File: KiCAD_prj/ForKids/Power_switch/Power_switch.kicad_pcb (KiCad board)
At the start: 2 copper layers, 61 x 33 mm, 19 parts, among them J1 Screw_Terminal_01x02, J2 Conn_01x04_Female, J3 Conn_01x04_Female, J4 Conn_01x04_Female, J5 Conn_01x04_Female, J6 Conn_01x04_Female, J7 Conn_01x04_Female, SW1 SW_SPST, U1 AMS1117-3.3, U2 AMS1117-5.0

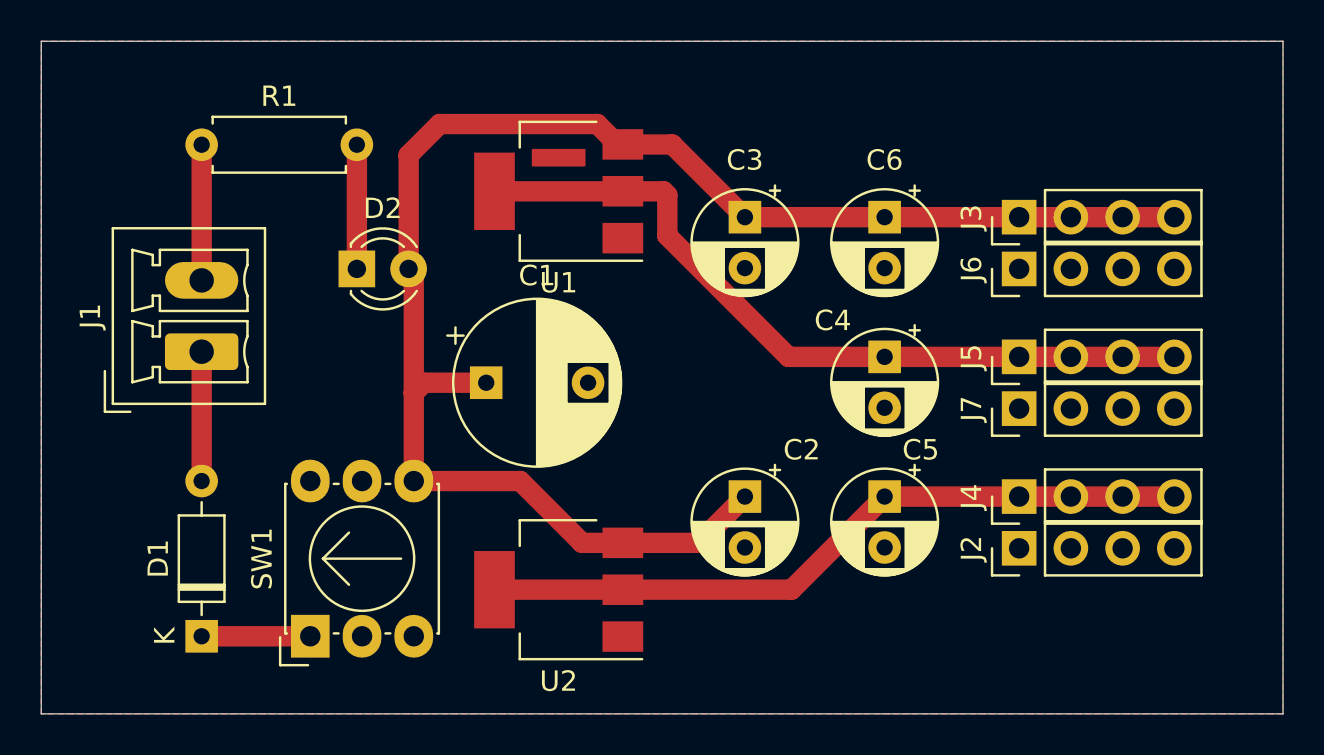
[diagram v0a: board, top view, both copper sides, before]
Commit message: Update Power Switch project KiCAD
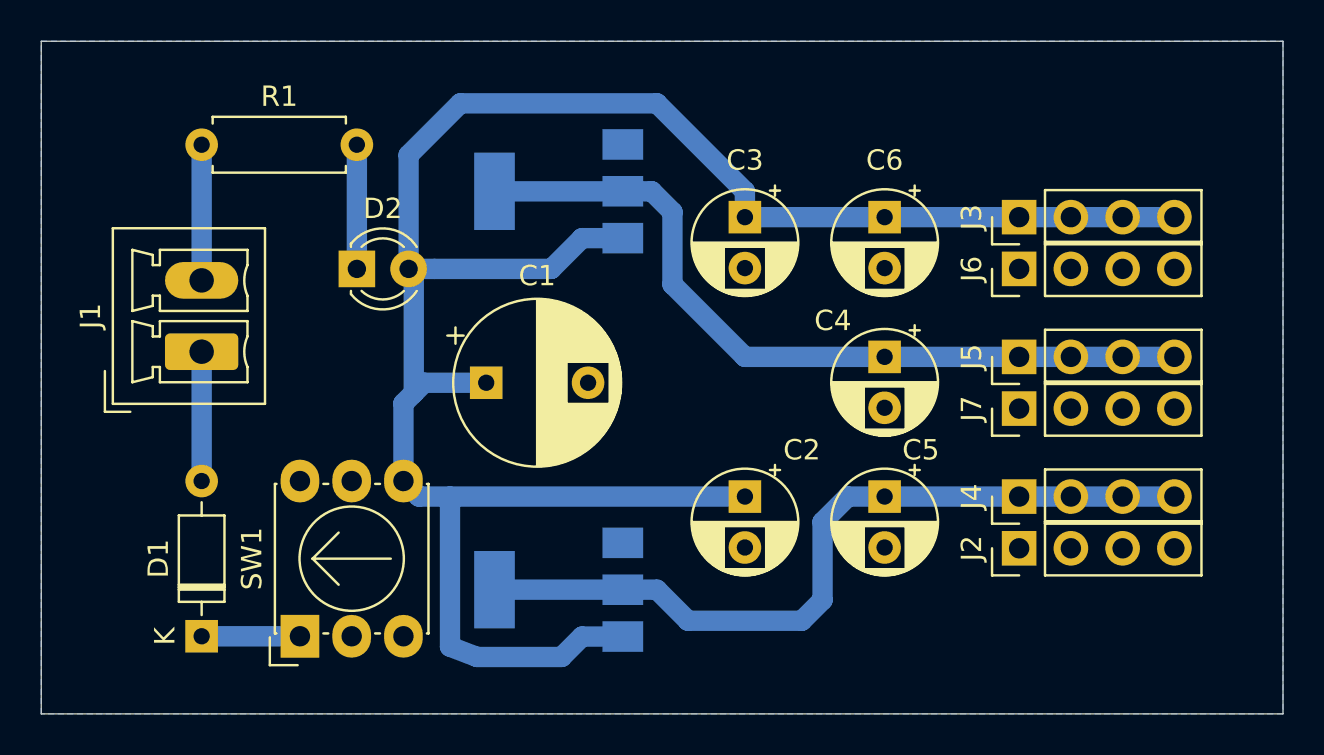
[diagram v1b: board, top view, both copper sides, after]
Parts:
- U1, U2: moved to B.Cu
- moved SW1 0.51 mm to (12.7, -3.81)
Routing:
- net VCC: track 78.4 -> 106.4 mm
- net Net-(C5-Pad1): track 35.3 -> 38.1 mm
- net Net-(C4-Pad1): track 37.9 -> 38.8 mm
- net Net-(D1-Pad1): track 5.33 -> 4.83 mm
- added copper zone on B.Cu, net Earth
- removed copper zone on F.Cu, net Earth

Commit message: Many changes
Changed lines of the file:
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@@
   (layers
     (0 F.Cu signal hide)
-    (31 B.Cu signal)
+    (31 B.Cu signal hide)
     (32 B.Adhes user hide)
     (33 F.Adhes user hide)
@@
       (effects (font (size 1 1) (thickness 0.15)))
     )
-    (fp_text value 10uF (at 1.25 3.75 90) (layer F.Fab)
+    (fp_text value 10uF (at -4.572 0.254 180) (layer F.Fab)
       (effects (font (size 1 1) (thickness 0.15)))
     )
@@
       (effects (font (size 1 1) (thickness 0.15)))
     )
-    (fp_text value 10uF (at 1.25 3.75 90) (layer F.Fab)
+    (fp_text value 10uF (at 5.588 -0.254 180) (layer F.Fab)
       (effects (font (size 1 1) (thickness 0.15)))
     )
@@
     (descr "Through hole straight pin header, 1x04, 2.54mm pitch, single row")
     (tags "Through hole pin header THT 1x04 2.54mm single row")
-    (fp_text reference J7 (at 0 -2.33 90) (layer F.SilkS)
+    (fp_text reference J7 (at 0 -2.794 180) (layer F.SilkS)
       (effects (font (size 1 1) (thickness 0.15)))
     )
@@
       (effects (font (size 1 1) (thickness 0.15)))
     )
-    (fp_text user %R (at 0 3.81) (layer F.Fab)
+    (fp_text user %R (at 0 3.81) (layer F.Fab) hide
       (effects (font (size 1 1) (thickness 0.15)))
     )
@@
     (descr "Through hole straight pin header, 1x04, 2.54mm pitch, single row")
     (tags "Through hole pin header THT 1x04 2.54mm single row")
-    (fp_text reference J6 (at 0 -2.33 90) (layer F.SilkS)
+    (fp_text reference J6 (at 0 -2.794 180) (layer F.SilkS)
       (effects (font (size 1 1) (thickness 0.15)))
     )
@@
       (effects (font (size 1 1) (thickness 0.15)))
     )
-    (fp_text user %R (at 0 3.81) (layer F.Fab)
+    (fp_text user %R (at 0 3.81) (layer F.Fab) hide
       (effects (font (size 1 1) (thickness 0.15)))
     )
@@
     (descr "Through hole straight pin header, 1x04, 2.54mm pitch, single row")
     (tags "Through hole pin header THT 1x04 2.54mm single row")
-    (fp_text reference J5 (at 0 -2.33 90) (layer F.SilkS)
+    (fp_text reference J5 (at 0 -2.794 180) (layer F.SilkS)
       (effects (font (size 1 1) (thickness 0.15)))
     )
@@
       (effects (font (size 1 1) (thickness 0.15)))
     )
-    (fp_text user %R (at 0 3.81) (layer F.Fab)
+    (fp_text user %R (at 0 3.81) (layer F.Fab) hide
       (effects (font (size 1 1) (thickness 0.15)))
     )
@@
     (descr "Through hole straight pin header, 1x04, 2.54mm pitch, single row")
     (tags "Through hole pin header THT 1x04 2.54mm single row")
-    (fp_text reference J4 (at 0 -2.33 90) (layer F.SilkS)
+    (fp_text reference J4 (at 0 -2.794 180) (layer F.SilkS)
       (effects (font (size 1 1) (thickness 0.15)))
     )
@@
       (effects (font (size 1 1) (thickness 0.15)))
     )
-    (fp_text user %R (at 0 3.81) (layer F.Fab)
+    (fp_text user %R (at 0 3.81) (layer F.Fab) hide
       (effects (font (size 1 1) (thickness 0.15)))
     )
@@
     (descr "Through hole straight pin header, 1x04, 2.54mm pitch, single row")
     (tags "Through hole pin header THT 1x04 2.54mm single row")
-    (fp_text reference J3 (at 0 -2.33 90) (layer F.SilkS)
+    (fp_text reference J3 (at 0 -2.794 180) (layer F.SilkS)
       (effects (font (size 1 1) (thickness 0.15)))
     )
@@
       (effects (font (size 1 1) (thickness 0.15)))
     )
-    (fp_text user %R (at 0 3.81) (layer F.Fab)
+    (fp_text user %R (at 0 3.81) (layer F.Fab) hide
       (effects (font (size 1 1) (thickness 0.15)))
     )
@@
     (descr "Through hole straight pin header, 1x04, 2.54mm pitch, single row")
     (tags "Through hole pin header THT 1x04 2.54mm single row")
-    (fp_text reference J2 (at 0 -2.33 90) (layer F.SilkS)
+    (fp_text reference J2 (at 0 -2.794 180) (layer F.SilkS)
       (effects (font (size 1 1) (thickness 0.15)))
     )
@@
       (effects (font (size 1 1) (thickness 0.15)))
     )
-    (fp_text user %R (at 0 3.81) (layer F.Fab)
+    (fp_text user %R (at 0 3.81) (layer F.Fab) hide
       (effects (font (size 1 1) (thickness 0.15)))
     )
@@
       (effects (font (size 1 1) (thickness 0.15)))
     )
-    (fp_text value SW_SPST (at 3.81 7.44 90) (layer F.Fab)
-      (effects (font (size 1 1) (thickness 0.15)))
-    )
-    (fp_text user %R (at 3.81 2.54 90) (layer F.Fab)
+    (fp_text value SW_SPST (at 3.81 7.44 90) (layer F.Fab) hide
+      (effects (font (size 1 1) (thickness 0.15)))
+    )
+    (fp_text user %R (at 3.556 8.382 180) (layer F.Fab)
       (effects (font (size 1 1) (thickness 0.15)))
     )
@@
     (descr "Generic Phoenix Contact connector footprint for: MCV_1,5/2-G-3.5; number of pins: 02; pin pitch: 3.50mm; Vertical || order number: 1843606 8A 160V")
     (tags "phoenix_contact connector MCV_01x02_G_3.5mm")
-    (fp_text reference J1 (at 1.75 -5.45 90) (layer F.SilkS)
+    (fp_text reference J1 (at 1.75 -5.45 180) (layer F.SilkS)
       (effects (font (size 1 1) (thickness 0.15)))
     )
@@
       (effects (font (size 1 1) (thickness 0.15)))
     )
-    (fp_text user %R (at 1.75 -3.55 90) (layer F.Fab)
+    (fp_text user %R (at 1.75 -3.55 90) (layer F.Fab) hide
       (effects (font (size 1 1) (thickness 0.15)))
     )
@@
       (effects (font (size 1 1) (thickness 0.15)))
     )
-    (fp_text value 1N4148 (at 4.318 -3.81 90) (layer F.Fab)
+    (fp_text value 1N4148 (at 9.906 0.254 180) (layer F.Fab)
       (effects (font (size 1 1) (thickness 0.15)))
     )
@@
       (effects (font (size 1 1) (thickness 0.15)))
     )
-    (fp_text value 22uF (at 1.25 3.75 90) (layer F.Fab)
+    (fp_text value 22uF (at -4.572 0 180) (layer F.Fab)
       (effects (font (size 1 1) (thickness 0.15)))
     )
@@
       (effects (font (size 1 1) (thickness 0.15)))
     )
-    (fp_text value 22uF (at 1.25 3.75 90) (layer F.Fab)
+    (fp_text value 22uF (at 5.588 -0.508 180) (layer F.Fab)
       (effects (font (size 1 1) (thickness 0.15)))
     )
@@
       (effects (font (size 1 1) (thickness 0.15)))
     )
-    (fp_text value 22uF (at 1.25 3.75 90) (layer F.Fab)
-      (effects (font (size 1 1) (thickness 0.15)))
-    )
+    (fp_text value 22uF (at 1.25 5.08 180) (layer F.Fab)
+      (effects (font (size 1 1) (thickness 0.15)))
+    )
